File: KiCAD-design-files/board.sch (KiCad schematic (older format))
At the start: 63 parts, among them IC1 TPS61025, P1 CONN_01X04, SW1 PTS820 J15M SMTR LFS, SW2 PTS820 J15M SMTR LFS, SW3 PTS820 J15M SMTR LFS, U1 ESP8266-ESP-03, U2 TPL5111, U3 MCP3021, U4 HDC1080, U5 LPS25HB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

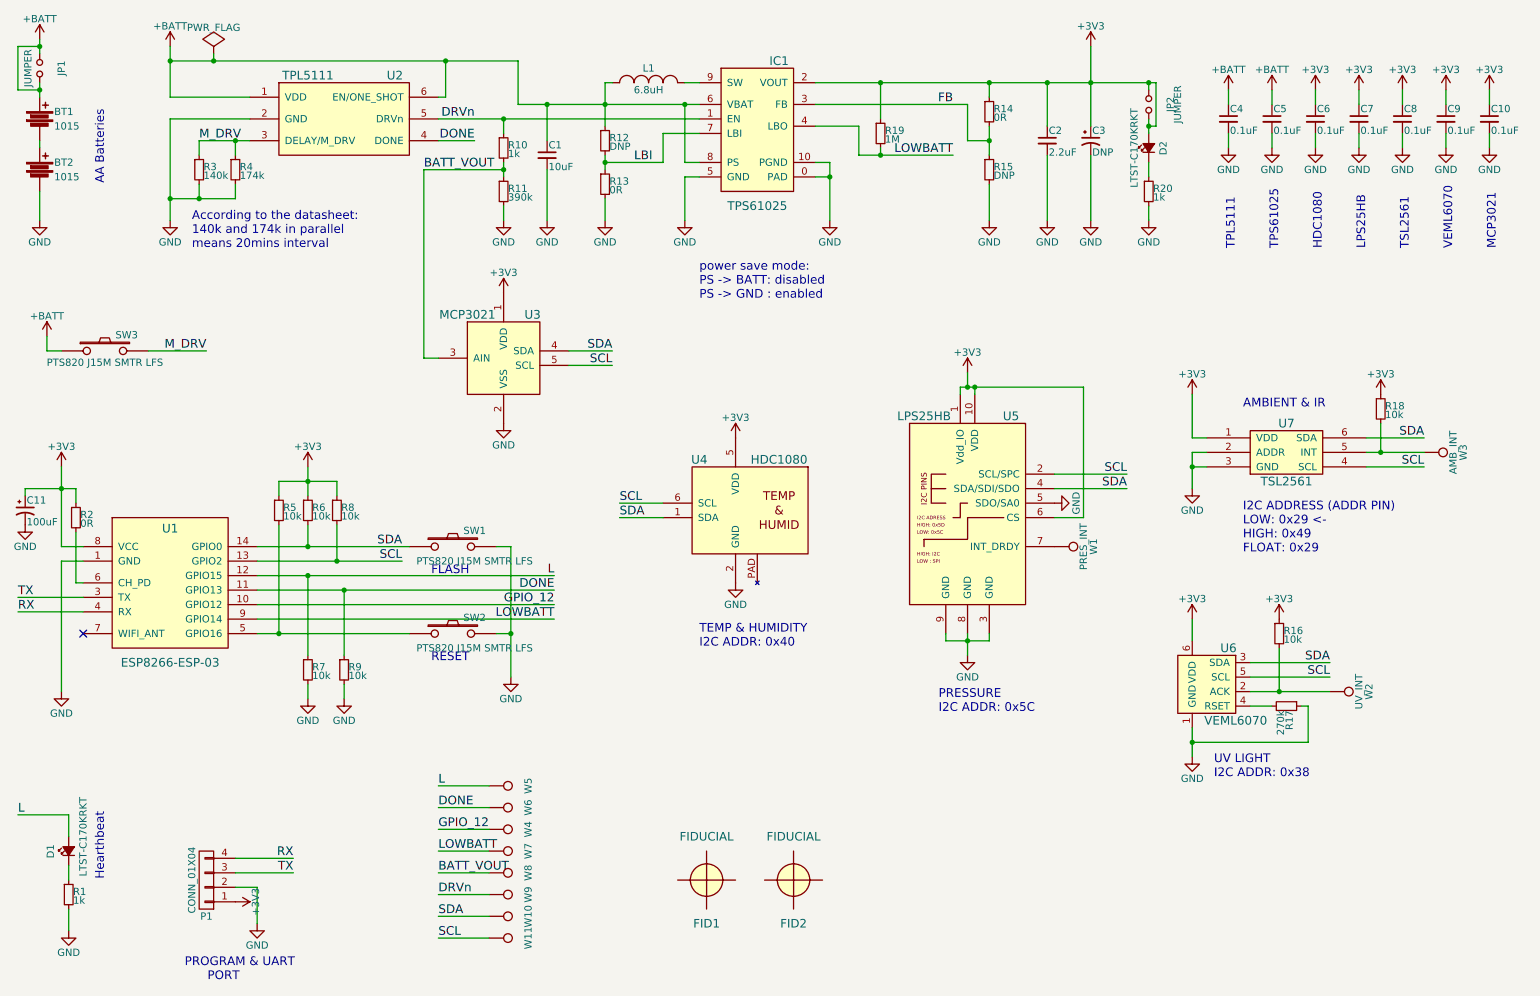
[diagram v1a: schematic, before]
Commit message: Some improvements & 3D CAD files added
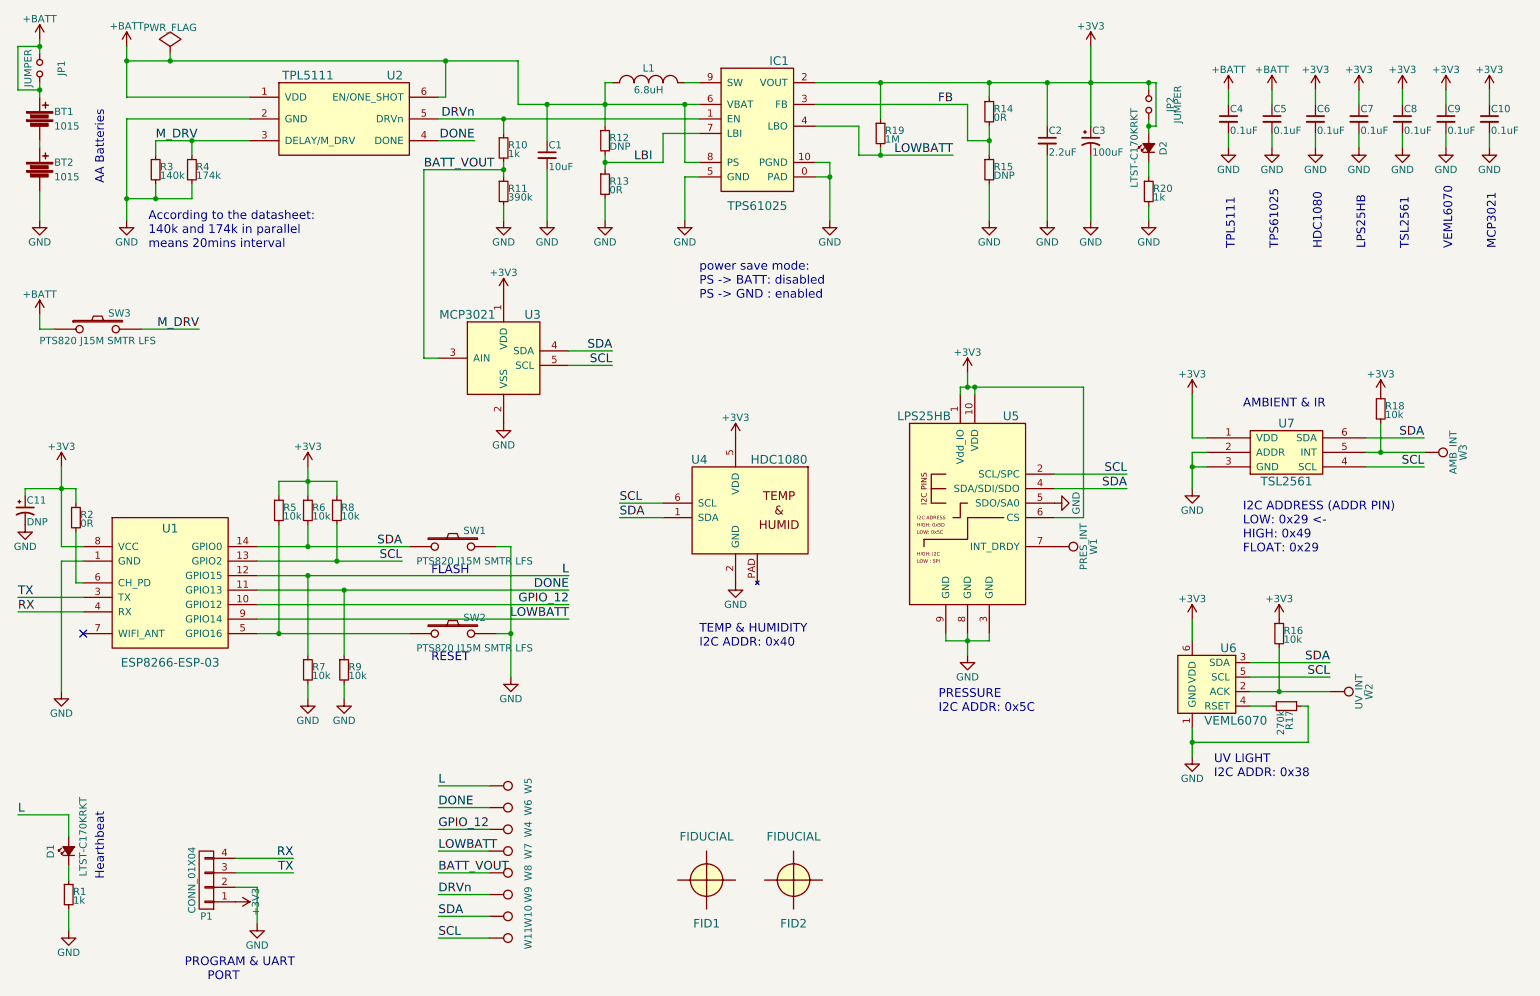
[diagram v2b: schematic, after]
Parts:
- C11: value 100uF -> DNP
- C3: value DNP -> 100uF
- L1: footprint footprints:Tayo_Yuden_NR40xx -> footprints:Inductor_1210; kicost:ignore (none) -> false
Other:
- moved on the sheet: R3, R4, SW3
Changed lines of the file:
@@
 F 0 "L1" H 5150 1550 50  0000 C CNN
 F 1 "6.8uH" H 5150 1400 50  0000 C CNN
-F 2 "footprints:Tayo_Yuden_NR40xx" H 5150 1450 50  0001 C CNN
+F 2 "footprints:Inductor_1210" H 5150 1450 50  0001 C CNN
 F 3 "" H 5150 1450 50  0000 C CNN
-F 4 "LQH32PN6R8NN0L" H 5150 1450 60  0001 C CNN "kicost:Manf#"
-F 5 "Murata Electronics" H 5150 1450 60  0001 C CNN "kicost:Manf"
+F 4 "Murata Electronics" H 5150 1450 60  0001 C CNN "kicost:Manf"
+F 5 "LQH32PN6R8NN0L" H 5150 1450 60  0001 C CNN "kicost:Manf#"
 F 6 "FIXED IND 6.8UH 850MA 240 MOHM" H 5150 1450 60  0001 C CNN "kicost:Desc"
+F 7 "false" H 5150 1450 60  0001 C CNN "kicost:ignore"
 	1    5150 1450
 	1    0    0    -1
@@
 L +BATT #PWR06
 U 1 1 5826237E
-P 1850 1200
-F 0 "#PWR06" H 1850 1050 50  0001 C CNN
-F 1 "+BATT" H 1850 1340 50  0000 C CNN
-F 2 "" H 1850 1200 50  0000 C CNN
-F 3 "" H 1850 1200 50  0000 C CNN
-	1    1850 1200
+P 1550 1200
+F 0 "#PWR06" H 1550 1050 50  0001 C CNN
+F 1 "+BATT" H 1550 1340 50  0000 C CNN
+F 2 "" H 1550 1200 50  0000 C CNN
+F 3 "" H 1550 1200 50  0000 C CNN
+	1    1550 1200
 	1    0    0    -1
 $EndComp
@@
 P 8200 1850
 F 0 "C3" H 8210 1920 50  0000 L CNN
-F 1 "DNP" H 8210 1770 50  0000 L CNN
+F 1 "100uF" H 8210 1770 50  0000 L CNN
 F 2 "footprints:TantalC_SizeB_EIA-3528_Reflow" H 8200 1850 50  0001 C CNN
 F 3 "" H 8200 1850 50  0000 C CNN
@@
 L R_Small R4
 U 1 1 58274F1B
-P 2300 2050
-F 0 "R4" H 2330 2070 50  0000 L CNN
-F 1 "174k" H 2330 2010 50  0000 L CNN
-F 2 "footprints:R_0603" H 2300 2050 50  0001 C CNN
-F 3 "" H 2300 2050 50  0000 C CNN
-F 4 "Yageo" H 2300 2050 60  0001 C CNN "kicost:Manf"
-F 5 "RC0603FR-07174KL" H 2300 2050 60  0001 C CNN "kicost:Manf#"
-F 6 "RES SMD 174K OHM 1% 1/10W 0603" H 2300 2050 60  0001 C CNN "kicost:Desc"
-F 7 "false" H 2300 2050 60  0001 C CNN "kicost:ignore"
-	1    2300 2050
+P 2000 2050
+F 0 "R4" H 2030 2070 50  0000 L CNN
+F 1 "174k" H 2030 2010 50  0000 L CNN
+F 2 "footprints:R_0603" H 2000 2050 50  0001 C CNN
+F 3 "" H 2000 2050 50  0000 C CNN
+F 4 "Yageo" H 2000 2050 60  0001 C CNN "kicost:Manf"
+F 5 "RC0603FR-07174KL" H 2000 2050 60  0001 C CNN "kicost:Manf#"
+F 6 "RES SMD 174K OHM 1% 1/10W 0603" H 2000 2050 60  0001 C CNN "kicost:Desc"
+F 7 "false" H 2000 2050 60  0001 C CNN "kicost:ignore"
+	1    2000 2050
 	1    0    0    -1
 $EndComp
@@
 L R_Small R3
 U 1 1 58274FDB
-P 2050 2050
-F 0 "R3" H 2080 2070 50  0000 L CNN
-F 1 "140k" H 2080 2010 50  0000 L CNN
-F 2 "footprints:R_0603" H 2050 2050 50  0001 C CNN
-F 3 "" H 2050 2050 50  0000 C CNN
-F 4 "Yageo" H 2050 2050 60  0001 C CNN "kicost:Manf"
-F 5 "RC0603FR-07140KL" H 2050 2050 60  0001 C CNN "kicost:Manf#"
-F 6 "RES SMD 140K OHM 1% 1/10W 0603" H 2050 2050 60  0001 C CNN "kicost:Desc"
-F 7 "false" H 2050 2050 60  0001 C CNN "kicost:ignore"
-	1    2050 2050
+P 1750 2050
+F 0 "R3" H 1780 2070 50  0000 L CNN
+F 1 "140k" H 1780 2010 50  0000 L CNN
+F 2 "footprints:R_0603" H 1750 2050 50  0001 C CNN
+F 3 "" H 1750 2050 50  0000 C CNN
+F 4 "Yageo" H 1750 2050 60  0001 C CNN "kicost:Manf"
+F 5 "RC0603FR-07140KL" H 1750 2050 60  0001 C CNN "kicost:Manf#"
+F 6 "RES SMD 140K OHM 1% 1/10W 0603" H 1750 2050 60  0001 C CNN "kicost:Desc"
+F 7 "false" H 1750 2050 60  0001 C CNN "kicost:ignore"
+	1    1750 2050
 	1    0    0    -1
 $EndComp
@@
 L GND #PWR016
 U 1 1 5827537F
-P 1850 2400
-F 0 "#PWR016" H 1850 2150 50  0001 C CNN
-F 1 "GND" H 1850 2250 50  0000 C CNN
-F 2 "" H 1850 2400 50  0000 C CNN
-F 3 "" H 1850 2400 50  0000 C CNN
-	1    1850 2400
+P 1550 2400
+F 0 "#PWR016" H 1550 2150 50  0001 C CNN
+F 1 "GND" H 1550 2250 50  0000 C CNN
+F 2 "" H 1550 2400 50  0000 C CNN
+F 3 "" H 1550 2400 50  0000 C CNN
+	1    1550 2400
 	1    0    0    -1
 $EndComp
@@
 	1    0    0    -1
 $EndComp
-Text Label 4500 4950 2    60   ~ 0
+Text Label 4600 4950 2    60   ~ 0
 DONE
-Text Notes 2000 2600 0    60   ~ 0
+Text Notes 1700 2600 0    60   ~ 0
 According to the datasheet:\n140k and 174k in parallel\nmeans 20mins interval
 Text Label 7250 1950 2    60   ~ 0
@@
 	0    1    1    0
 $EndComp
-Text Label 4500 4850 2    60   ~ 0
+Text Label 4600 4850 2    60   ~ 0
 L
 $Comp
@@
 Text Notes 5500 5350 0    60   ~ 0
 TEMP & HUMIDITY\nI2C ADDR: 0x40
-Text Label 4500 5150 2    60   ~ 0
+Text Label 4600 5150 2    60   ~ 0
 LOWBATT
 $Comp
@@
 L PWR_FLAG #FLG050
 U 1 1 582A4BAD
-P 2150 1250
-F 0 "#FLG050" H 2150 1345 50  0001 C CNN
-F 1 "PWR_FLAG" H 2150 1430 50  0000 C CNN
-F 2 "" H 2150 1250 50  0000 C CNN
-F 3 "" H 2150 1250 50  0000 C CNN
-	1    2150 1250
+P 1850 1250
+F 0 "#FLG050" H 1850 1345 50  0001 C CNN
+F 1 "PWR_FLAG" H 1850 1430 50  0000 C CNN
+F 2 "" H 1850 1250 50  0000 C CNN
+F 3 "" H 1850 1250 50  0000 C CNN
+	1    1850 1250
 	1    0    0    -1
 $EndComp
@@
 P 850 4400
 F 0 "C11" H 860 4470 50  0000 L CNN
-F 1 "100uF" H 860 4320 50  0000 L CNN
+F 1 "DNP" H 860 4320 50  0000 L CNN
 F 2 "footprints:TantalC_SizeB_EIA-3528_Reflow" H 850 4400 50  0001 C CNN
 F 3 "" H 850 4400 50  0000 C CNN
@@
 L SW_PUSH SW3
 U 1 1 582ABB2E
-P 1400 3300
-F 0 "SW3" H 1550 3410 50  0000 C CNN
-F 1 "PTS820 J15M SMTR LFS" H 1400 3220 50  0000 C CNN
-F 2 "footprints:Tact_Switch_Top_PTS820" H 1400 3300 50  0001 C CNN
-F 3 "" H 1400 3300 50  0000 C CNN
-F 4 "C&K" H 1400 3300 60  0001 C CNN "kicost:Manf"
-F 5 "PTS820 J15M SMTR LFS" H 1400 3300 60  0001 C CNN "kicost:Manf#"
-F 6 "SWITCH TACTILE SPST-NO 0.05A 12V" H 1400 3300 60  0001 C CNN "kicost:Desc"
-F 7 "false" H 1400 3300 60  0001 C CNN "kicost:ignore"
-	1    1400 3300
+P 1350 3150
+F 0 "SW3" H 1500 3260 50  0000 C CNN
+F 1 "PTS820 J15M SMTR LFS" H 1350 3070 50  0000 C CNN
+F 2 "footprints:Tact_Switch_Top_PTS820" H 1350 3150 50  0001 C CNN
+F 3 "" H 1350 3150 50  0000 C CNN
+F 4 "C&K" H 1350 3150 60  0001 C CNN "kicost:Manf"
+F 5 "PTS820 J15M SMTR LFS" H 1350 3150 60  0001 C CNN "kicost:Manf#"
+F 6 "SWITCH TACTILE SPST-NO 0.05A 12V" H 1350 3150 60  0001 C CNN "kicost:Desc"
+F 7 "false" H 1350 3150 60  0001 C CNN "kicost:ignore"
+	1    1350 3150
 	1    0    0    -1
 $EndComp
@@
 L +BATT #PWR052
 U 1 1 582ABC3D
-P 1000 3200
-F 0 "#PWR052" H 1000 3050 50  0001 C CNN
-F 1 "+BATT" H 1000 3340 50  0000 C CNN
-F 2 "" H 1000 3200 50  0000 C CNN
-F 3 "" H 1000 3200 50  0000 C CNN
-	1    1000 3200
+P 950 3050
+F 0 "#PWR052" H 950 2900 50  0001 C CNN
+F 1 "+BATT" H 950 3190 50  0000 C CNN
+F 2 "" H 950 3050 50  0000 C CNN
+F 3 "" H 950 3050 50  0000 C CNN
+	1    950  3050
 	1    0    0    -1
 $EndComp
-Text Label 2100 3300 2    60   ~ 0
+Text Label 2050 3150 2    60   ~ 0
 M_DRV
-Text Label 2050 1850 0    60   ~ 0
+Text Label 1750 1850 0    60   ~ 0
 M_DRV
 $Comp
@@
 	1    0    0    -1
 $EndComp
-Text Label 4500 5050 2    60   ~ 0
+Text Label 4600 5050 2    60   ~ 0
 GPIO_12
 $Comp
@@
 	4450 2050 4450 2400
 Wire Wire Line
-	1850 1200 1850 1550
+	1550 1200 1550 1550
 Wire Wire Line
 	5250 1800 5500 1800
@@
 	2800 5400 2800 4850
 Wire Wire Line
-	2450 4850 4500 4850
+	2450 4850 4600 4850
 Wire Wire Line
 	2800 5600 2800 5700
@@
 	3700 1850 3950 1850
 Wire Wire Line
-	2050 1950 2050 1850
+	1750 1950 1750 1850
 Wire Wire Line
-	2050 1850 2400 1850
+	1750 1850 2400 1850
 Wire Wire Line
-	2300 1950 2300 1850
-Connection ~ 2300 1850
+	2000 1950 2000 1850
+Connection ~ 2000 1850
 Wire Wire Line
-	2050 2150 2050 2250
+	1750 2150 1750 2250
 Wire Wire Line
-	1850 2250 2300 2250
+	1550 2250 2000 2250
 Wire Wire Line
-	2300 2250 2300 2150
+	2000 2250 2000 2150
 Wire Wire Line
-	2400 1700 1850 1700
+	2400 1700 1550 1700
 Wire Wire Line
-	1850 1700 1850 2400
-Connection ~ 2050 2250
+	1550 1700 1550 2400
+Connection ~ 1750 2250
 Wire Wire Line
 	4450 1600 4450 1850
 Wire Wire Line
-	1850 1550 2400 1550
-Connection ~ 1850 1300
+	1550 1550 2400 1550
+Connection ~ 1550 1300
 Connection ~ 4450 1600
 Wire Wire Line
 	950  2200 950  2400
 Wire Wire Line
-	1850 1300 4250 1300
+	1550 1300 4250 1300
 Wire Wire Line
 	9150 1500 9150 1600
@@
 Connection ~ 2800 4850
 Connection ~ 3000 4750
-Connection ~ 1850 2250
+Connection ~ 1550 2250
 Wire Wire Line
 	9750 1800 9750 1900
@@
 	7950 4250 8450 4250
 Wire Wire Line
-	2450 4950 4500 4950
+	2450 4950 4600 4950
 Wire Wire Line
 	3050 5400 3050 4950
@@
 	1150 7150 1150 7300
 Wire Wire Line
-	2450 5150 4500 5150
+	2450 5150 4600 5150
 Wire Wire Line
 	10950 1800 10950 1900
@@
 	4600 3400 4900 3400
 Wire Wire Line
-	2150 1250 2150 1300
-Connection ~ 2150 1300
+	1850 1250 1850 1300
+Connection ~ 1850 1300
 Wire Wire Line
-	2450 5050 4500 5050
+	2450 5050 4600 5050
 Wire Wire Line
 	850  4300 850  4250
@@
 Connection ~ 6750 1450
 Wire Wire Line
-	1000 3200 1000 3300
+	950  3050 950  3150
 Wire Wire Line
-	1000 3300 1100 3300
+	950  3150 1050 3150
 Wire Wire Line
-	1700 3300 2100 3300
+	1650 3150 2050 3150
 Wire Wire Line
 	8600 2000 8600 2100
